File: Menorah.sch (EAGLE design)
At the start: 34 parts

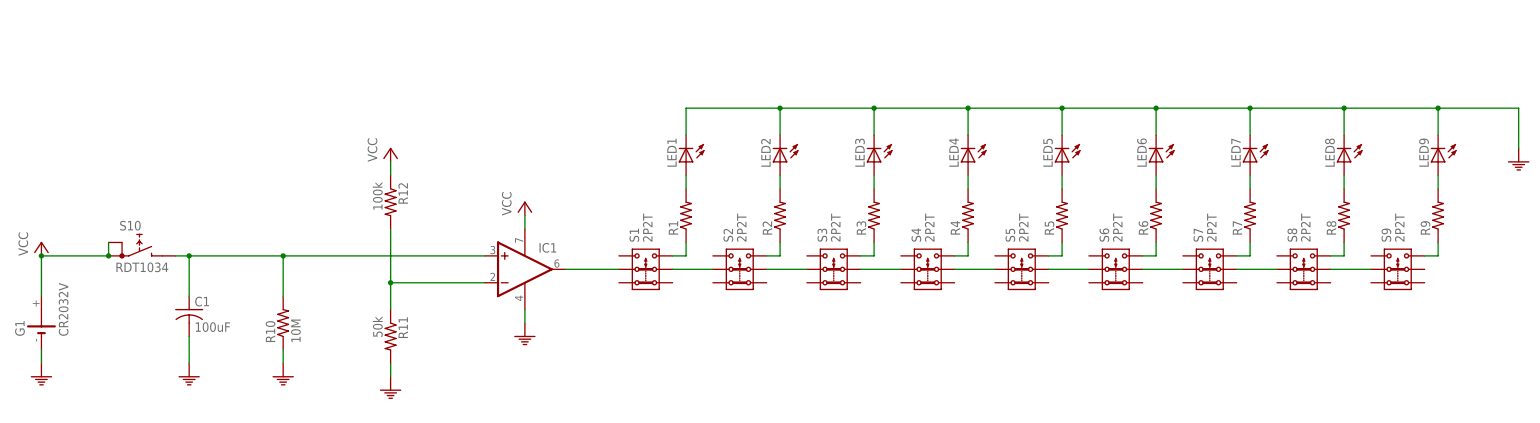
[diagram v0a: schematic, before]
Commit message: digikey part numbers added
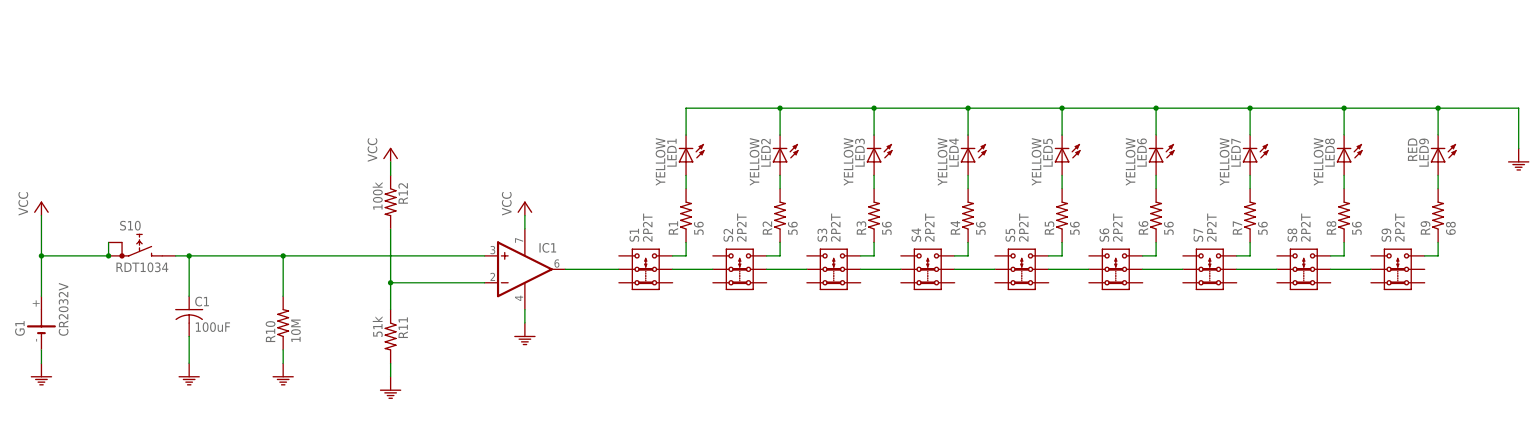
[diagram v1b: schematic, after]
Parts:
- C1: device rcl:C-USC1808 -> rcl:C-USC1206; DIGIKEY (none) -> 490-4539-1-ND
- G1: DIGIKEY (none) -> BK-913-ND
- IC1: DIGIKEY (none) -> MCP6001UT-I/OTCT-ND
- LED1, LED2, LED3, LED4, LED5, LED6, LED7, LED8: value (none) -> YELLOW; device led:LEDP-LCC-4 -> led:LEDCHIPLED_0805; DIGIKEY (none) -> 475-2560-1-ND
- LED9: value (none) -> RED; device led:LEDP-LCC-4 -> led:LEDCHIPLED_0805; DIGIKEY (none) -> 475-1415-1-ND
- R1, R2, R3, R4, R5, R6, R7, R8: value (none) -> 56; DIGIKEY (none) -> 1276-5502-1-ND
- R10: DIGIKEY (none) -> 1276-5617-1-ND
- R11: value 50k -> 51k; DIGIKEY (none) -> 1276-5569-1-ND
- R12: DIGIKEY (none) -> 1276-5576-1-ND
- R9: value (none) -> 68; DIGIKEY (none) -> 1276-5504-1-ND
- S1, S2, S3, S4, S5, S6, S7, S8, S9: DIGIKEY (none) -> 401-2002-1-ND
- S10: DIGIKEY (none) -> EG4791-ND

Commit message: replaced cr2032
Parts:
- G1: value CR2032V -> CR2032; device battery:CR2032V -> Menorah:CR2032; LAYOUT-VERIFIED (none) -> No
- S10: LAYOUT-VERIFIED (none) -> No
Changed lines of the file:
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@@
 </part>
 <part name="GND" library="supply1" deviceset="PE" device=""/>
-<part name="G1" library="battery" deviceset="CR2032V" device="">
+<part name="G1" library="Menorah" deviceset="CR2032" device="">
 <attribute name="DIGIKEY" value="BK-913-ND"/>
+<attribute name="LAYOUT-VERIFIED" value="No"/>
 </part>
 <part name="GND1" library="supply1" deviceset="PE" device=""/>
 <part name="S10" library="switch" deviceset="RDT1034" device="">
 <attribute name="DIGIKEY" value="EG4791-ND"/>
+<attribute name="LAYOUT-VERIFIED" value="No"/>
 </part>
 <part name="C1" library="rcl" deviceset="C-US" device="C1206" value="100uF">
@@
 </instance>
 <instance part="GND" gate="M" x="327.66" y="152.4" smashed="yes"/>
-<instance part="G1" gate="1" x="48.26" y="121.92" rot="R90">
+<instance part="G1" gate="G$1" x="48.26" y="121.92" rot="R90">
 <attribute name="DIGIKEY" x="48.26" y="121.92" size="1.778" layer="96" rot="R90" display="off"/>
+<attribute name="LAYOUT-VERIFIED" x="48.26" y="121.92" size="1.778" layer="96" rot="R90" display="off"/>
 </instance>
 <instance part="GND1" gate="M" x="48.26" y="111.76" smashed="yes"/>
 <instance part="S10" gate="G$1" x="66.04" y="137.16">
 <attribute name="DIGIKEY" x="66.04" y="137.16" size="1.778" layer="96" display="off"/>
+<attribute name="LAYOUT-VERIFIED" x="66.04" y="137.16" size="1.778" layer="96" display="off"/>
 </instance>
 <instance part="C1" gate="G$1" x="76.2" y="124.46">
@@
 <segment>
 <pinref part="GND1" gate="M" pin="PE"/>
-<pinref part="G1" gate="1" pin="-"/>
+<pinref part="G1" gate="G$1" pin="-"/>
 <wire x1="48.26" y1="114.3" x2="48.26" y2="116.84" width="0.1524" layer="91"/>
 </segment>
@@
 <net name="VCC" class="0">
 <segment>
-<pinref part="G1" gate="1" pin="+"/>
+<pinref part="G1" gate="G$1" pin="+"/>
 <wire x1="48.26" y1="142.24" x2="48.26" y2="134.62" width="0.1524" layer="91"/>
 <pinref part="P+1" gate="VCC" pin="VCC"/>

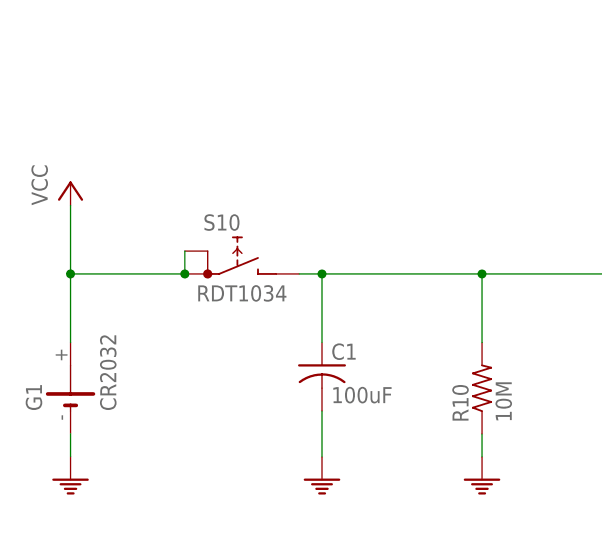
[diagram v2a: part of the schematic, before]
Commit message: replaced spst switch
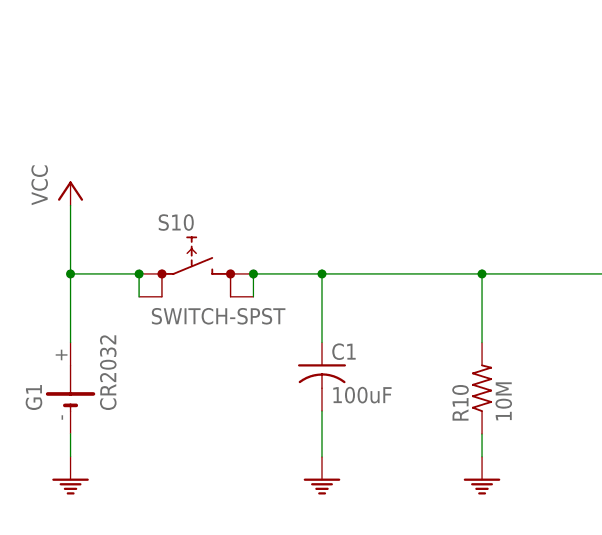
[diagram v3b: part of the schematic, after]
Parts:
- G1: LAYOUT-VERIFIED No -> (none)
- S10: value RDT1034 -> SWITCH-SPST; device switch:RDT1034 -> Menorah:SWITCH-SPST; DIGIKEY EG4791-ND -> (none); LAYOUT-VERIFIED No -> (none)
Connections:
- removed net N$20: C1.1, IC1.+IN, R10.2, S10.B
- new net N$22: C1.1, IC1.+IN, R10.2, S10.1@A, S10.1@B
- net VCC: now also S10.0@A, S10.0@B; no longer S10.A, S10.A1
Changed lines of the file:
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@@
 <part name="G1" library="Menorah" deviceset="CR2032" device="">
 <attribute name="DIGIKEY" value="BK-913-ND"/>
-<attribute name="LAYOUT-VERIFIED" value="No"/>
 </part>
 <part name="GND1" library="supply1" deviceset="PE" device=""/>
-<part name="S10" library="switch" deviceset="RDT1034" device="">
-<attribute name="DIGIKEY" value="EG4791-ND"/>
-<attribute name="LAYOUT-VERIFIED" value="No"/>
-</part>
 <part name="C1" library="rcl" deviceset="C-US" device="C1206" value="100uF">
 <attribute name="DIGIKEY" value="490-4539-1-ND"/>
@@
 <attribute name="DIGIKEY" value="401-2002-1-ND"/>
 </part>
+<part name="S10" library="Menorah" deviceset="SWITCH-SPST" device=""/>
 </parts>
 <sheets>
@@
 <instance part="G1" gate="G$1" x="48.26" y="121.92" rot="R90">
 <attribute name="DIGIKEY" x="48.26" y="121.92" size="1.778" layer="96" rot="R90" display="off"/>
-<attribute name="LAYOUT-VERIFIED" x="48.26" y="121.92" size="1.778" layer="96" rot="R90" display="off"/>
 </instance>
 <instance part="GND1" gate="M" x="48.26" y="111.76" smashed="yes"/>
-<instance part="S10" gate="G$1" x="66.04" y="137.16">
-<attribute name="DIGIKEY" x="66.04" y="137.16" size="1.778" layer="96" display="off"/>
-<attribute name="LAYOUT-VERIFIED" x="66.04" y="137.16" size="1.778" layer="96" display="off"/>
-</instance>
 <instance part="C1" gate="G$1" x="76.2" y="124.46">
 <attribute name="DIGIKEY" x="76.2" y="124.46" size="1.778" layer="96" display="off"/>
@@
 <attribute name="DIGIKEY" x="304.8" y="132.08" size="1.778" layer="96" rot="R90" display="off"/>
 </instance>
+<instance part="S10" gate="G$1" x="63.5" y="134.62"/>
 </instances>
 <busses>
@@
 </segment>
 </net>
-<net name="N$20" class="0">
-<segment>
-<pinref part="S10" gate="G$1" pin="B"/>
-<wire x1="73.66" y1="134.62" x2="76.2" y2="134.62" width="0.1524" layer="91"/>
-<pinref part="C1" gate="G$1" pin="1"/>
-<wire x1="76.2" y1="134.62" x2="76.2" y2="127" width="0.1524" layer="91"/>
-<pinref part="IC1" gate="A" pin="+IN"/>
-<wire x1="132.08" y1="134.62" x2="93.98" y2="134.62" width="0.1524" layer="91"/>
-<junction x="76.2" y="134.62"/>
-<pinref part="R10" gate="G$1" pin="2"/>
-<wire x1="93.98" y1="134.62" x2="76.2" y2="134.62" width="0.1524" layer="91"/>
-<wire x1="93.98" y1="127" x2="93.98" y2="134.62" width="0.1524" layer="91"/>
-<junction x="93.98" y="134.62"/>
-</segment>
-</net>
 <net name="VCC" class="0">
 <segment>
 <pinref part="G1" gate="G$1" pin="+"/>
+<pinref part="P+1" gate="VCC" pin="VCC"/>
 <wire x1="48.26" y1="142.24" x2="48.26" y2="134.62" width="0.1524" layer="91"/>
-<pinref part="P+1" gate="VCC" pin="VCC"/>
-<pinref part="S10" gate="G$1" pin="A1"/>
-<pinref part="S10" gate="G$1" pin="A"/>
+<pinref part="S10" gate="G$1" pin="0@A"/>
 <wire x1="48.26" y1="134.62" x2="48.26" y2="127" width="0.1524" layer="91"/>
-<wire x1="60.96" y1="137.16" x2="60.96" y2="134.62" width="0.1524" layer="91"/>
-<wire x1="60.96" y1="134.62" x2="48.26" y2="134.62" width="0.1524" layer="91"/>
-<junction x="60.96" y="134.62"/>
+<wire x1="55.88" y1="134.62" x2="48.26" y2="134.62" width="0.1524" layer="91"/>
 <junction x="48.26" y="134.62"/>
+<pinref part="S10" gate="G$1" pin="0@B"/>
+<wire x1="55.88" y1="132.08" x2="55.88" y2="134.62" width="0.1524" layer="91"/>
+<junction x="55.88" y="134.62"/>
 </segment>
 <segment>
@@
 </segment>
 </net>
+<net name="N$22" class="0">
+<segment>
+<pinref part="S10" gate="G$1" pin="1@B"/>
+<pinref part="S10" gate="G$1" pin="1@A"/>
+<wire x1="68.58" y1="132.08" x2="68.58" y2="134.62" width="0.1524" layer="91"/>
+<pinref part="C1" gate="G$1" pin="1"/>
+<wire x1="76.2" y1="134.62" x2="76.2" y2="127" width="0.1524" layer="91"/>
+<pinref part="IC1" gate="A" pin="+IN"/>
+<wire x1="132.08" y1="134.62" x2="93.98" y2="134.62" width="0.1524" layer="91"/>
+<pinref part="R10" gate="G$1" pin="2"/>
+<wire x1="93.98" y1="134.62" x2="76.2" y2="134.62" width="0.1524" layer="91"/>
+<wire x1="93.98" y1="127" x2="93.98" y2="134.62" width="0.1524" layer="91"/>
+<junction x="93.98" y="134.62"/>
+<wire x1="68.58" y1="134.62" x2="76.2" y2="134.62" width="0.1524" layer="91"/>
+<junction x="68.58" y="134.62"/>
+<junction x="76.2" y="134.62"/>
+</segment>
+</net>
